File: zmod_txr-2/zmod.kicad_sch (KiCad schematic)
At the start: 13 parts, among them J2 QTH-020-01-X-D-DP-A

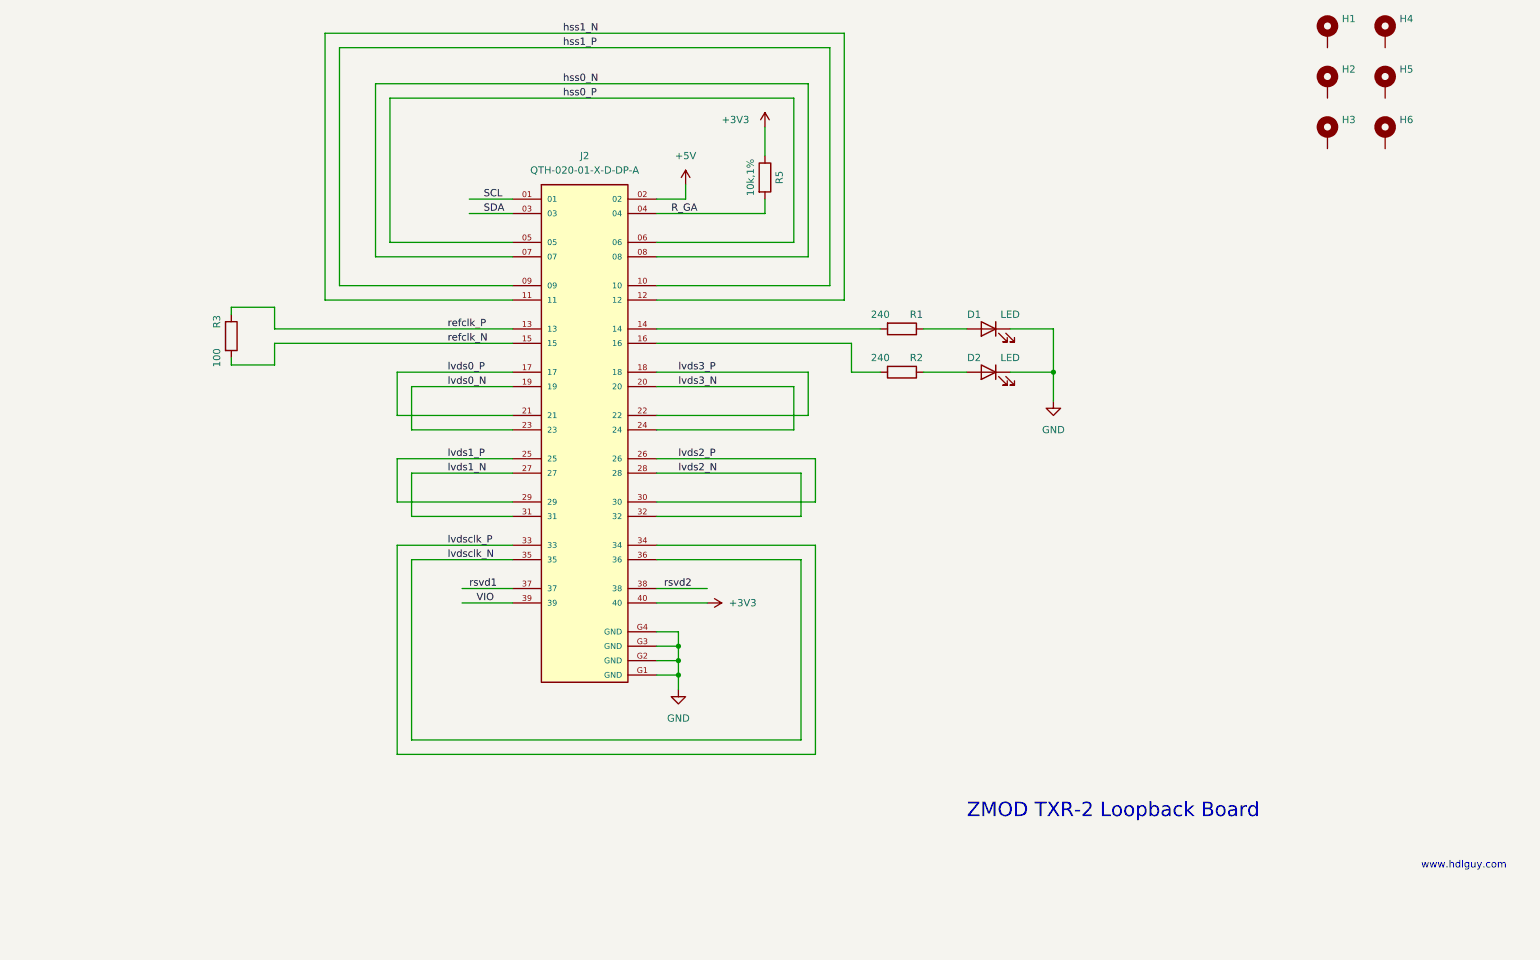
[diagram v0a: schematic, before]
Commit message: added M.2-m connector to the design for a sata ssd
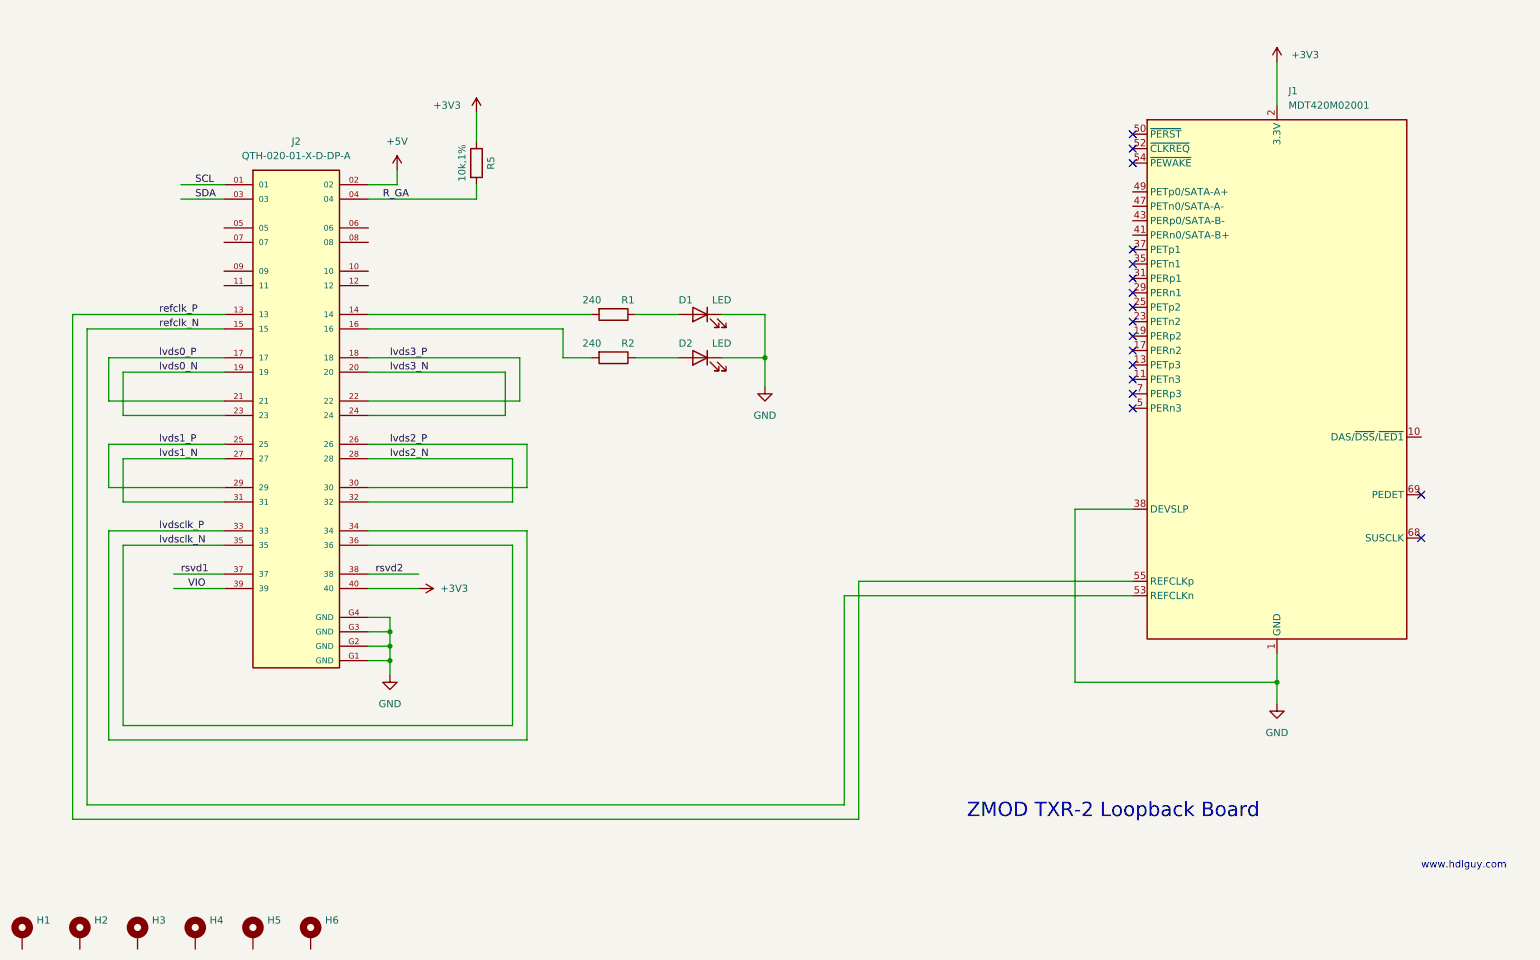
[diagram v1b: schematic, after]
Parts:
- removed R3: 100, Resistor_SMD:R_0603_1608Metric, symbol Device:R
- added J1: MDT420M02001, 1-2199230-5:TE_1-2199230-5, symbol pedrolib:MDT420M02001
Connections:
- net +3V3: now also J1.12 (3.3V), J1.14 (3.3V), J1.16 (3.3V), J1.18 (3.3V), J1.2 (3.3V), J1.4 (3.3V), J1.70 (3.3V), J1.72 (3.3V), J1.74 (3.3V)
- net GND: now also J1.1 (GND), J1.15 (GND), J1.21 (GND), J1.27 (GND), J1.3 (GND), J1.33 (GND), J1.38 (DEVSLP), J1.39 (GND), J1.45 (GND), J1.51 (GND), J1.57 (GND), J1.71 (GND), J1.73 (GND), J1.75 (GND), J1.9 (GND)
- net refclk_N: now also J1.53 (REFCLKn)
- net refclk_P: now also J1.55 (REFCLKp)
- net hss0_N: no longer names the net of J2.07
- net hss0_N: no longer J2.08
- net hss0_P: no longer names the net of J2.05
- net hss0_P: no longer J2.06
- net hss1_N: no longer names the net of J2.11
- net hss1_N: no longer J2.12
- net hss1_P: no longer names the net of J2.09
- net hss1_P: no longer J2.10
- no-connect marks 0 -> 17
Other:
- moved on the sheet: D1, D2, H1, H2, H3, H4, H5, H6, J2, R1, R2, R5

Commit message: organizing local libraries, footprint and symbol
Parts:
- J1: footprint 1-2199230-5:TE_1-2199230-5 -> pedrolib:TE_1-2199230-5
- J2: footprint SAMTEC_QTH-020-01-X-D-DP-A -> pedrolib:SAMTEC_QTH-020-01-X-D-DP-A; symbol QTH-020-01-X-D-DP-A:QTH-020-01-X-D-DP-A -> pedrolib:QTH-020-01-X-D-DP-A
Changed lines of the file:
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@@
     (pin "1")
   )
-  (symbol (lib_id "QTH-020-01-X-D-DP-A:QTH-020-01-X-D-DP-A") (at 66.04 97.79 0) (unit 1)
+  (symbol (lib_id "pedrolib:QTH-020-01-X-D-DP-A") (at 66.04 97.79 0) (unit 1)
     (in_bom yes) (on_board yes) (fields_autoplaced)
     (property "Reference" "J2" (id 0) (at 66.04 52.07 0))
     (property "Value" "QTH-020-01-X-D-DP-A" (id 1) (at 66.04 54.61 0))
-    (property "Footprint" "SAMTEC_QTH-020-01-X-D-DP-A" (id 2) (at 66.04 97.79 0)
+    (property "Footprint" "pedrolib:SAMTEC_QTH-020-01-X-D-DP-A" (id 2) (at 66.04 97.79 0)
       (effects (font (size 1.27 1.27)) (justify left bottom) hide)
     )
@@
       (effects (font (size 1.27 1.27)) (justify left))
     )
-    (property "Footprint" "1-2199230-5:TE_1-2199230-5" (id 2) (at 238.76 67.31 0)
+    (property "Footprint" "pedrolib:TE_1-2199230-5" (id 2) (at 238.76 67.31 0)
       (effects (font (size 1.27 1.27)) hide)
     )
@@
     )
     (path "/713a8cb6-be5c-413a-968b-156735b7e9f4"
-      (reference "J1") (unit 1) (value "MDT420M02001") (footprint "1-2199230-5:TE_1-2199230-5")
+      (reference "J1") (unit 1) (value "MDT420M02001") (footprint "pedrolib:TE_1-2199230-5")
     )
     (path "/0d6ebd58-e16b-44d9-a783-6f9c7178f556"
-      (reference "J2") (unit 1) (value "QTH-020-01-X-D-DP-A") (footprint "SAMTEC_QTH-020-01-X-D-DP-A")
+      (reference "J2") (unit 1) (value "QTH-020-01-X-D-DP-A") (footprint "pedrolib:SAMTEC_QTH-020-01-X-D-DP-A")
     )
     (path "/ff644ff7-2624-41c7-a7cc-9f9e7511816f"

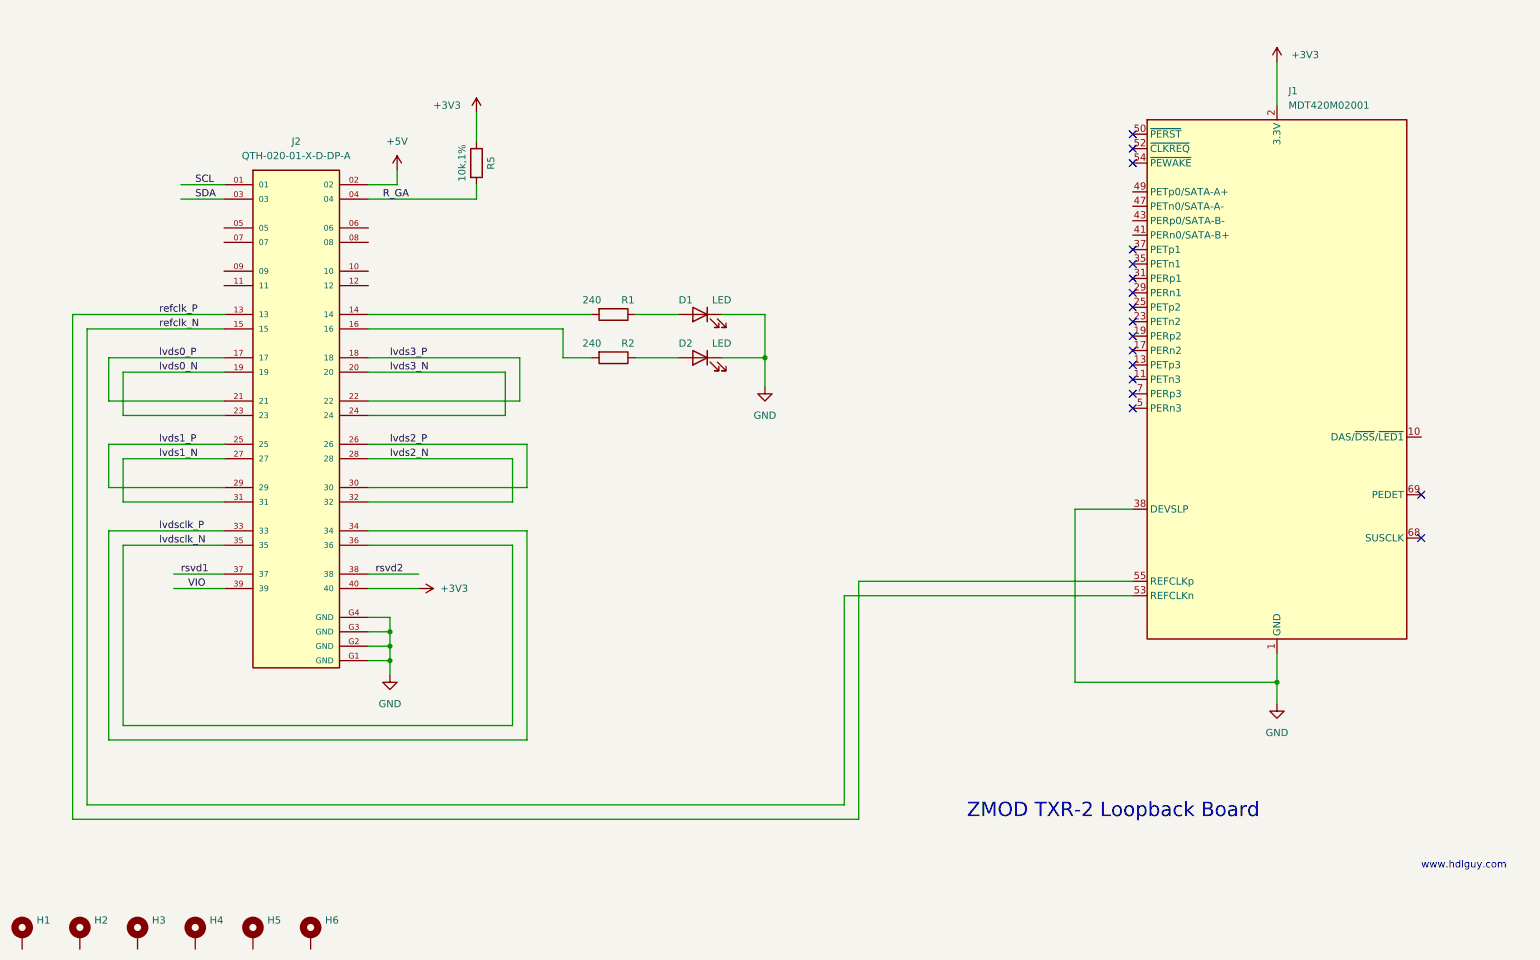
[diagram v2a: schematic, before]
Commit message: working on M.2 ZMOD board
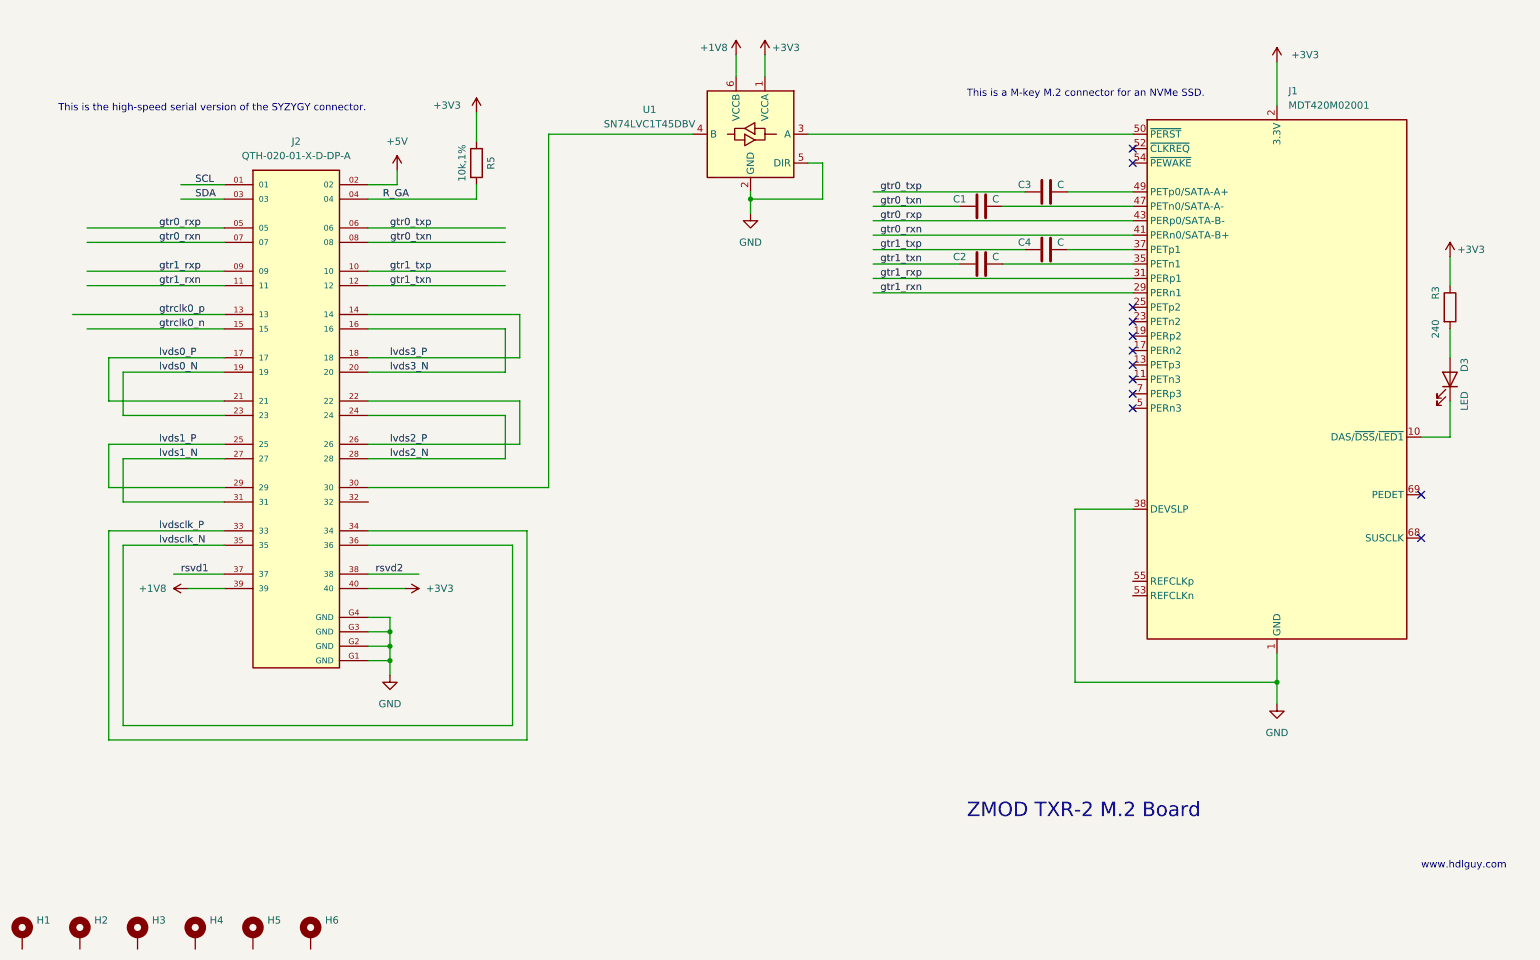
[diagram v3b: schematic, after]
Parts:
- removed D1, D2: LED, LED_SMD:LED_0603_1608Metric, symbol Device:LED
- removed R1, R2: 240, Resistor_SMD:R_0603_1608Metric, symbol Device:R
- added C1, C2, C3, C4: C, Capacitor_SMD:C_0603_1608Metric, symbol Device:C
- added D3: LED, LED_SMD:LED_0603_1608Metric, symbol Device:LED
- added R3: 240, Resistor_SMD:R_0603_1608Metric, symbol Device:R
- added U1: SN74LVC1T45DBV, Package_TO_SOT_SMD:SOT-23-6, symbol Logic_LevelTranslator:SN74LVC1T45DBV
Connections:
- net +3V3: now also R3.1, U1.1 (VCCA)
- net GND: now also U1.2 (GND), U1.5 (DIR)
- net lvds2_N: now also J2.24; no longer J2.32
- net lvds2_P: now also J2.22; no longer J2.30
- net lvds3_N: now also J2.16; no longer J2.24
- net lvds3_P: now also J2.14; no longer J2.22
- net gtr0_rxp: now reaches J2.05
- net gtr0_rxp: now also J1.43 (PERp0/SATA-B-)
- net gtr0_txp: now reaches J2.06
- net gtr0_txp: now also C3.1
- net gtr0_rxn: now reaches J2.07
- net gtr0_rxn: now also J1.41 (PERn0/SATA-B+)
- net gtr0_txn: now reaches J2.08
- net gtr0_txn: now also C1.1
- net gtr1_rxp: now reaches J2.09
- net gtr1_rxp: now also J1.31 (PERp1)
- net gtr1_txp: now reaches J2.10
- net gtr1_txp: now also C4.1
- net gtr1_rxn: now reaches J2.11
- net gtr1_rxn: now also J1.29 (PERn1)
- net gtr1_txn: now reaches J2.12
- net gtr1_txn: now also C2.1
- net at J1.10 (DAS/~{DSS}/~{LED1}): now also D3.1 (K)
- net at J1.35 (PETn1): now also C2.2
- net at J1.37 (PETp1): now also C4.2
- net at J1.47 (PETn0/SATA-A-): now also C1.2
- net at J1.49 (PETp0/SATA-A+): now also C3.2
- net at J1.50 (~{PERST}): now also U1.3 (A)
- net VIO renamed +1V8
- net +1V8: now also U1.6 (VCCB)
- net refclk_N: no longer names the net of J1.53 (REFCLKn)
- net refclk_N: no longer J2.15
- net refclk_P: no longer names the net of J1.55 (REFCLKp)
- net refclk_P: no longer J2.13
- new net: J2.30, U1.4 (B)
- new net: D3.2 (A), R3.2
- new net gtrclk0_n: J2.15
- new net gtrclk0_p: J2.13
- no-connect marks 17 -> 12
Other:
- note added: "This is a M-key M.2 connector for an NVMe SSD."
- note added: "This is the high-speed serial version of the SYZYGY connector."
- note added: "ZMOD TXR-2 M.2 Board"
- note removed: "ZMOD TXR-2 Loopback Board"
